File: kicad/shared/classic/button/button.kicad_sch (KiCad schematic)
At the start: 9 parts, among them J2 Conn_01x04, Q1 BC547

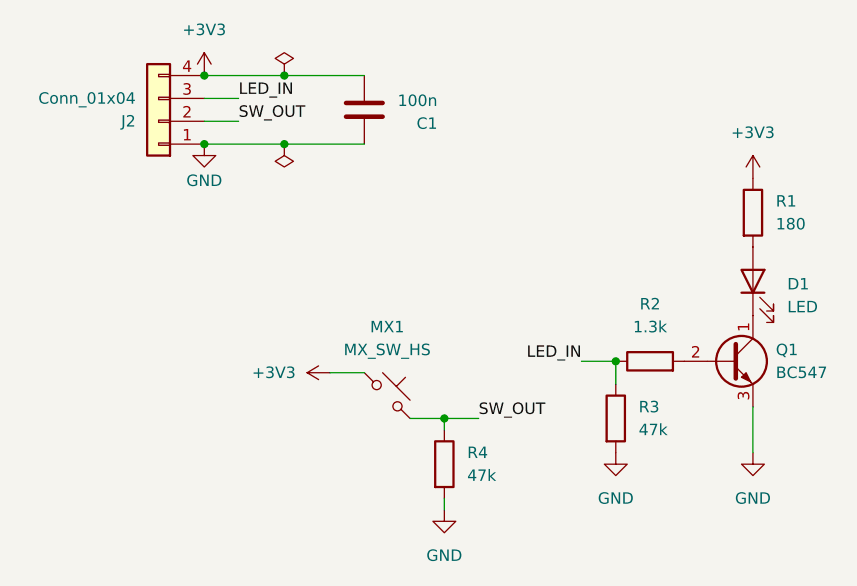
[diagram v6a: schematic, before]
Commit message: feat: Should be able to footprint and route some prototype boards to see if I'm not totally off-base here
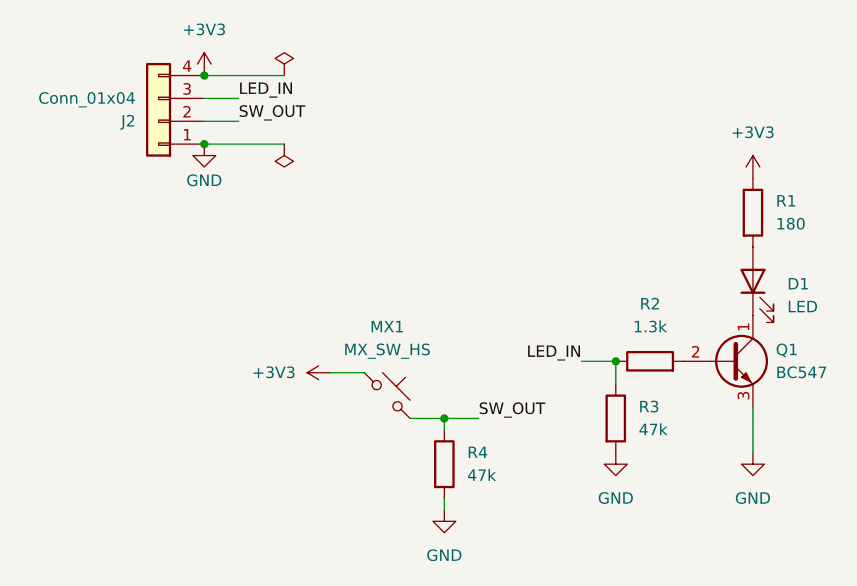
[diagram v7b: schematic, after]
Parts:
- removed C1: 100n, Capacitor_SMD:C_0805_2012Metric, symbol Device:C
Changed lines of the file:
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@@
-	)
-	(junction
-		(at 41.91 48.26)
-		(diameter 0)
-		(color 0 0 0 0)
 	)
 	(junction
@@
 	)
 	(junction
-		(at 41.91 55.88)
-		(diameter 0)
-		(color 0 0 0 0)
-	)
-	(junction
 		(at 78.74 80.01)
 		(diameter 0)
@@
 	(wire
 		(pts
+			(xy 74.93 80.01) (xy 78.74 80.01)
+		)
+		(stroke
+			(width 0)
+			(type default)
+		)
+	)
+	(wire
+		(pts
 			(xy 33.02 55.88) (xy 41.91 55.88)
 		)
@@
 	(wire
 		(pts
-			(xy 74.93 80.01) (xy 78.74 80.01)
-		)
-		(stroke
-			(width 0)
-			(type default)
-		)
-	)
-	(wire
-		(pts
 			(xy 59.69 95.25) (xy 59.69 96.52)
 		)
@@
 	(wire
 		(pts
-			(xy 41.91 48.26) (xy 50.8 48.26)
-		)
-		(stroke
-			(width 0)
-			(type default)
-		)
-	)
-	(wire
-		(pts
 			(xy 36.83 53.34) (xy 33.02 53.34)
 		)
@@
 		(pts
 			(xy 59.69 86.36) (xy 59.69 87.63)
-		)
-		(stroke
-			(width 0)
-			(type default)
-		)
-	)
-	(wire
-		(pts
-			(xy 41.91 55.88) (xy 50.8 55.88)
 		)
 		(stroke
@@
 			)
 			(justify right bottom)
-		)
-	)
-	(symbol
-		(lib_id "power:PWR_FLAG")
-		(at 41.91 48.26 0)
-		(unit 1)
-		(body_style 1)
-		(exclude_from_sim no)
-		(in_bom yes)
-		(on_board yes)
-		(in_pos_files yes)
-		(dnp no)
-		(property "Reference" "#FLG01"
-			(at 41.91 46.355 0)
-			(hide yes)
-			(show_name no)
-			(do_not_autoplace no)
-			(effects
-				(font
-					(size 1.27 1.27)
-				)
-			)
-		)
-		(property "Value" "PWR_FLAG"
-			(at 40.64 44.704 90)
-			(hide yes)
-			(show_name no)
-			(do_not_autoplace no)
-			(effects
-				(font
-					(size 1.27 1.27)
-				)
-				(justify left)
-			)
-		)
-		(property "Footprint" ""
-			(at 41.91 48.26 0)
-			(hide yes)
-			(show_name no)
-			(do_not_autoplace no)
-			(effects
-				(font
-					(size 1.27 1.27)
-				)
-			)
-		)
-		(property "Datasheet" ""
-			(at 41.91 48.26 0)
-			(hide yes)
-			(show_name no)
-			(do_not_autoplace no)
-			(effects
-				(font
-					(size 1.27 1.27)
-				)
-			)
-		)
-		(property "Description" "Special symbol for telling ERC where power comes from"
-			(at 41.91 48.26 0)
-			(hide yes)
-			(show_name no)
-			(do_not_autoplace no)
-			(effects
-				(font
-					(size 1.27 1.27)
-				)
-			)
-		)
-		(pin "1"
-		)
-		(instances
-			(project "button"
-				(path "/9bcb4978-1926-4e41-8c2f-efd6bcbfb6f8"
-					(reference "#FLG01")
-					(unit 1)
-				)
-			)
 		)
 	)
@@
 	)
 	(symbol
-		(lib_id "Device:C")
-		(at 50.8 52.07 180)
-		(unit 1)
-		(body_style 1)
-		(exclude_from_sim no)
-		(in_bom yes)
-		(on_board yes)
-		(in_pos_files yes)
-		(dnp no)
-		(property "Reference" "C1"
-			(at 58.928 53.594 0)
-			(show_name no)
-			(do_not_autoplace no)
-			(effects
-				(font
-					(size 1.27 1.27)
-				)
-				(justify left)
-			)
-		)
-		(property "Value" "100n"
-			(at 58.928 51.054 0)
-			(show_name no)
-			(do_not_autoplace no)
-			(effects
-				(font
-					(size 1.27 1.27)
-				)
-				(justify left)
-			)
-		)
-		(property "Footprint" "Capacitor_SMD:C_0805_2012Metric"
-			(at 49.8348 48.26 0)
-			(hide yes)
-			(show_name no)
-			(do_not_autoplace no)
-			(effects
-				(font
-					(size 1.27 1.27)
-				)
-			)
-		)
-		(property "Datasheet" ""
-			(at 50.8 52.07 0)
-			(hide yes)
-			(show_name no)
-			(do_not_autoplace no)
-			(effects
-				(font
-					(size 1.27 1.27)
-				)
-			)
-		)
-		(property "Description" "Unpolarized capacitor"
-			(at 50.8 52.07 0)
-			(hide yes)
-			(show_name no)
-			(do_not_autoplace no)
-			(effects
-				(font
-					(size 1.27 1.27)
-				)
-			)
-		)
-		(pin "2"
-		)
-		(pin "1"
-		)
-		(instances
-			(project "button"
-				(path "/9bcb4978-1926-4e41-8c2f-efd6bcbfb6f8"
-					(reference "C1")
-					(unit 1)
-				)
-			)
-		)
-	)
-	(symbol
 		(lib_id "Device:LED")
 		(at 93.98 71.12 90)
@@
 					(unit 1)
 				)
+			)
+		)
+	)
+	(symbol
+		(lib_id "power:PWR_FLAG")
+		(at 41.91 48.26 0)
+		(unit 1)
+		(body_style 1)
+		(exclude_from_sim no)
+		(in_bom yes)
+		(on_board yes)
+		(in_pos_files yes)
+		(dnp no)
+		(fields_autoplaced yes)
+		(property "Reference" "#FLG03"
+			(at 41.91 46.355 0)
+			(hide yes)
+			(show_name no)
+			(do_not_autoplace no)
+			(effects
+				(font
+					(size 1.27 1.27)
+				)
+			)
+		)
+		(property "Value" "PWR_FLAG"
+			(at 41.91 43.18 0)
+			(hide yes)
+			(show_name no)
+			(do_not_autoplace no)
+			(effects
+				(font
+					(size 1.27 1.27)
+				)
+			)
+		)
+		(property "Footprint" ""
+			(at 41.91 48.26 0)
+			(hide yes)
+			(show_name no)
+			(do_not_autoplace no)
+			(effects
+				(font
+					(size 1.27 1.27)
+				)
+			)
+		)
+		(property "Datasheet" ""
+			(at 41.91 48.26 0)
+			(hide yes)
+			(show_name no)
+			(do_not_autoplace no)
+			(effects
+				(font
+					(size 1.27 1.27)
+				)
+			)
+		)
+		(property "Description" "Special symbol for telling ERC where power comes from"
+			(at 41.91 48.26 0)
+			(hide yes)
+			(show_name no)
+			(do_not_autoplace no)
+			(effects
+				(font
+					(size 1.27 1.27)
+				)
+			)
+		)
+		(pin "1"
+		)
+		(instances
+			(project "button"
+				(path "/9bcb4978-1926-4e41-8c2f-efd6bcbfb6f8"
+					(reference "#FLG03")
+					(unit 1)
+				)

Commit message: feat: Routed prototype THT component boards for buzzer and button/LED assembly PCBs
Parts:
- J2: footprint Connector_JST:JST_XA_B04B-XASK-1-A_1x04_P2.50mm_Vertical -> Connector_PinSocket_2.54mm:PinSocket_1x04_P2.54mm_Vertical
- R1, R2, R3, R4: footprint Resistor_SMD:R_0805_2012Metric -> Resistor_THT:R_Axial_DIN0207_L6.3mm_D2.5mm_P7.62mm_Horizontal
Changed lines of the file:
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@@
 			)
 		)
-		(property "Footprint" "Connector_JST:JST_XA_B04B-XASK-1-A_1x04_P2.50mm_Vertical"
+		(property "Footprint" "Connector_PinSocket_2.54mm:PinSocket_1x04_P2.54mm_Vertical"
 			(at 27.94 53.34 0)
 			(hide yes)
@@
 			)
 		)
-		(property "Footprint" "Resistor_SMD:R_0805_2012Metric"
+		(property "Footprint" "Resistor_THT:R_Axial_DIN0207_L6.3mm_D2.5mm_P7.62mm_Horizontal"
 			(at 76.962 86.36 90)
 			(hide yes)
@@
 			)
 		)
-		(property "Footprint" "Resistor_SMD:R_0805_2012Metric"
+		(property "Footprint" "Resistor_THT:R_Axial_DIN0207_L6.3mm_D2.5mm_P7.62mm_Horizontal"
 			(at 92.202 63.5 90)
 			(hide yes)
@@
 			)
 		)
-		(property "Footprint" "Resistor_SMD:R_0805_2012Metric"
+		(property "Footprint" "Resistor_THT:R_Axial_DIN0207_L6.3mm_D2.5mm_P7.62mm_Horizontal"
 			(at 57.912 91.44 90)
 			(hide yes)
@@
 			)
 		)
-		(property "Footprint" "Resistor_SMD:R_0805_2012Metric"
+		(property "Footprint" "Resistor_THT:R_Axial_DIN0207_L6.3mm_D2.5mm_P7.62mm_Horizontal"
 			(at 82.55 81.788 90)
 			(hide yes)
